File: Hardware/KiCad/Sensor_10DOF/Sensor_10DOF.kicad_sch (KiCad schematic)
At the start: 21 parts, among them U1 BMI160, U2 BME280, U3 LSM303AGR, U4 WeMos_D1_mini, U6 LP2985-3.3

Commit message: fast fertig. Pinbelegung prüfen
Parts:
- added J1: Conn_01x04, Connector_JST:JST_XA_B04B-XASK-1_1x04_P2.50mm_Vertical, symbol Connector_Generic:Conn_01x04
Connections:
- net +3.3V: now also J1.3 (Pin_3)
- net GND: now also J1.4 (Pin_4)
- net SCL: now also J1.1 (Pin_1)
- net SDA: now also J1.2 (Pin_2)
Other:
- moved on the sheet: C7, C8, U6

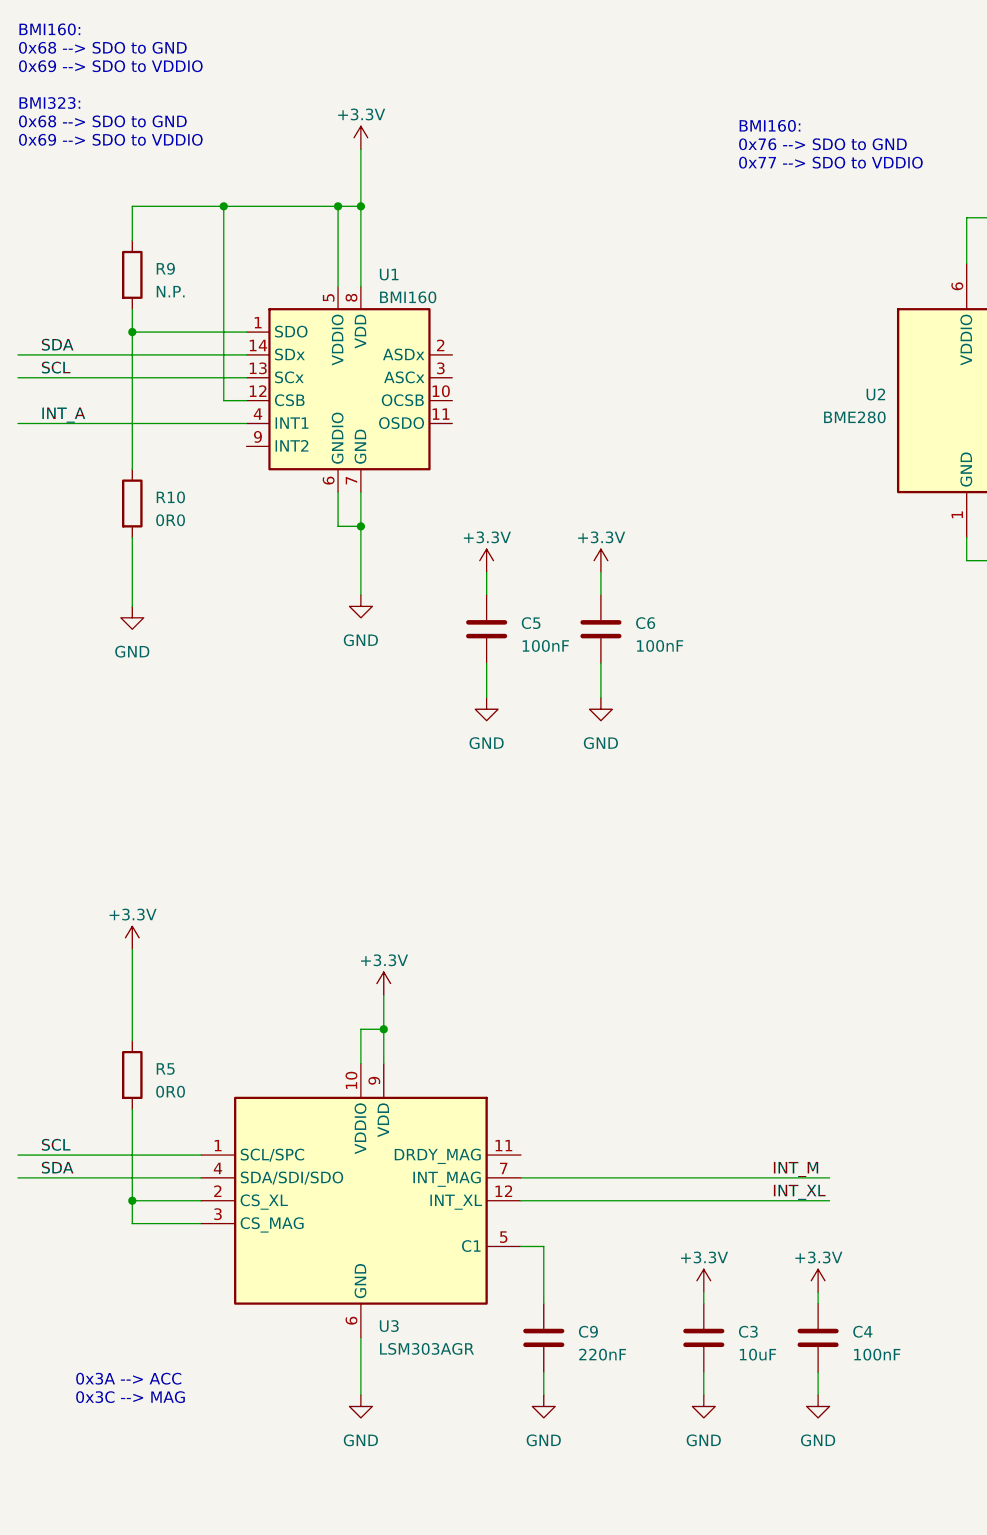
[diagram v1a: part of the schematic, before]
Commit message: Rename --> Sensor_10DOF.pdf pdf to schematic.pdf
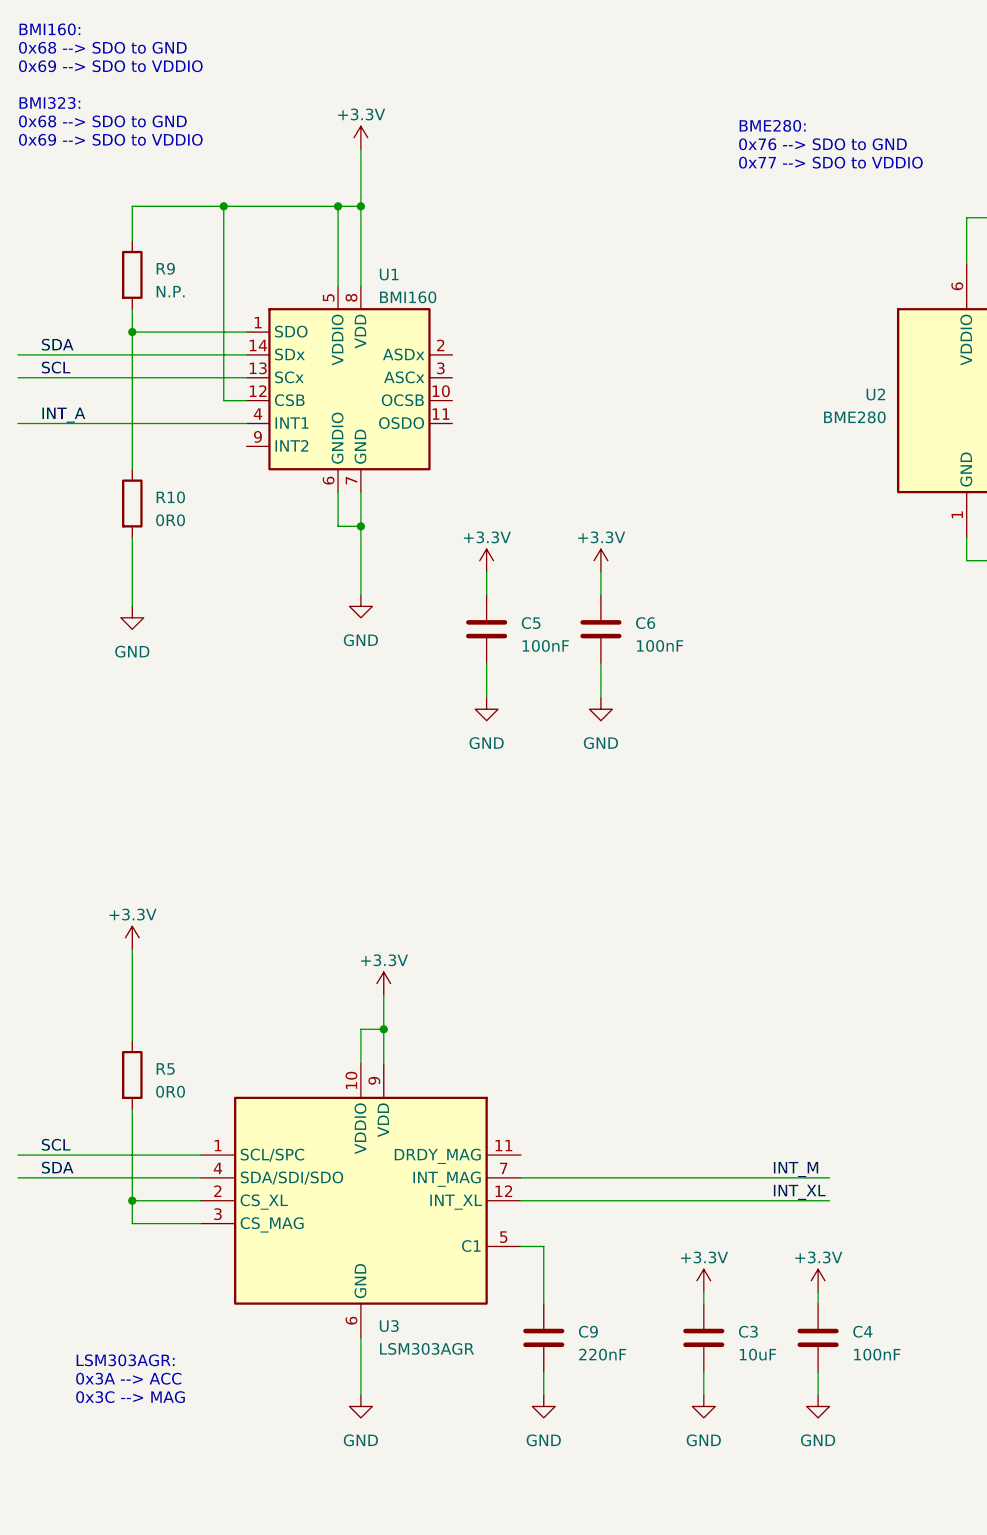
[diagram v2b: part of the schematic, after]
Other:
- note added: "BME280: 0x76 --> SDO to GND 0x77 --> SDO to VDDIO"
- note added: "LSM303AGR: 0x3A --> ACC 0x3C --> MAG"
- note removed: "0x3A --> ACC 0x3C --> MAG"
- note removed: "BMI160: 0x76 --> SDO to GND 0x77 --> SDO to VDDIO"
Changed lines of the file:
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@@
     (stroke (width 0) (type default))
   )
-  (text "BMI160:\n0x76 --> SDO to GND\n0x77 --> SDO to VDDIO" (at 118.11 53.34 0)
+  (text "BME280:\n0x76 --> SDO to GND\n0x77 --> SDO to VDDIO" (at 118.11 53.34 0)
     (effects (font (size 1.27 1.27)) (justify left bottom))
   )
@@
     (effects (font (size 1.27 1.27)) (justify left bottom))
   )
-  (text "0x3A --> ACC\n0x3C --> MAG" (at 44.45 190.5 0)
+  (text "LSM303AGR:\n0x3A --> ACC\n0x3C --> MAG" (at 44.45 190.5 0)
     (effects (font (size 1.27 1.27)) (justify left bottom))
   )

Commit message: version 1.0 - release Gerberdaten erzeugt
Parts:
- added C10: 1u, Capacitor_SMD:C_0603_1608Metric, symbol Device:C
- added R6: N.P., Resistor_SMD:R_0402_1005Metric, symbol Device:R
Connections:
- net +3.3V: now also R6.2; no longer J1.3 (Pin_3), U4.8 (3V3)
- net GND: now also J1.3 (Pin_3), C10.2; no longer J1.4 (Pin_4)
- net INT_A: now also U4.7 (CS/D8); no longer U4.3 (D0)
- net VBUS: now also J1.4 (Pin_4), C10.1
- new net: R6.1, U4.8 (3V3)

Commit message: bestückungsplan erstellt
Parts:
- R2, R6, R9: value N.P. -> DNP
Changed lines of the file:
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@@
       (effects (font (size 1.27 1.27)) (justify left))
     )
-    (property "Value" "N.P." (at 53.34 66.675 0)
+    (property "Value" "DNP" (at 53.34 66.675 0)
       (effects (font (size 1.27 1.27)) (justify left))
     )
@@
       (effects (font (size 1.27 1.27)))
     )
-    (property "Value" "N.P." (at 335.28 52.07 90)
+    (property "Value" "DNP" (at 335.28 52.07 90)
       (effects (font (size 1.27 1.27)))
     )
@@
       (effects (font (size 1.27 1.27)) (justify left))
     )
-    (property "Value" "N.P." (at 171.45 66.675 0)
-      (effects (font (size 1.27 1.27)) (justify left))
-    )
+    (property "Value" "DNP" (at 171.45 66.675 0)
+      (effects (font (size 1.27 1.27)) (justify left))
+    )
